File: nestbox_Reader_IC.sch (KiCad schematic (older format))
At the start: 45 parts, among them U2 ST95HF, Y2 ABM11-142-27.120MHz

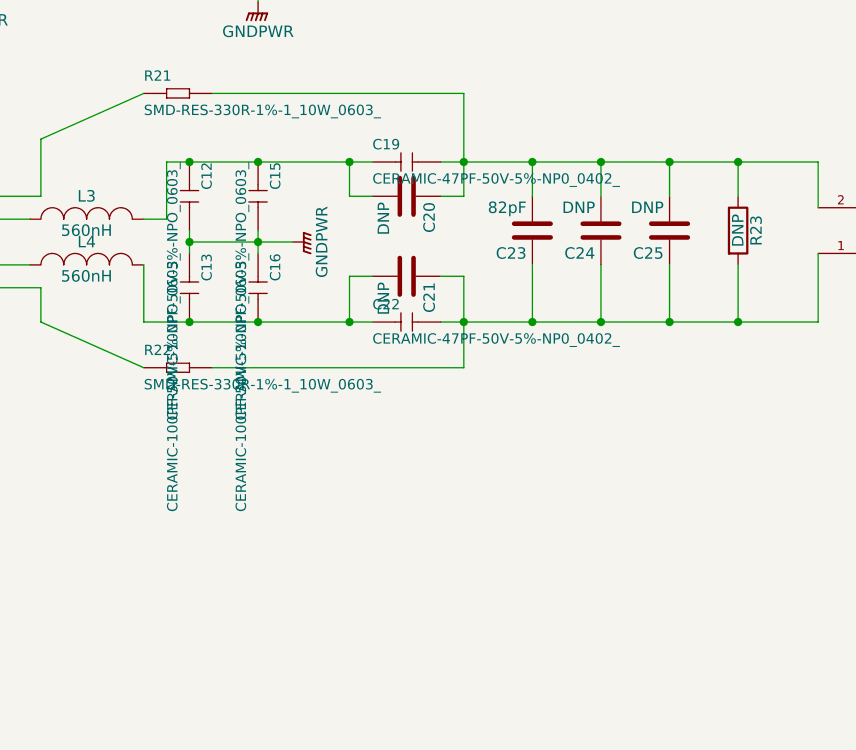
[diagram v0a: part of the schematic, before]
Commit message: Updated BOM with one version of the antenna matching network components
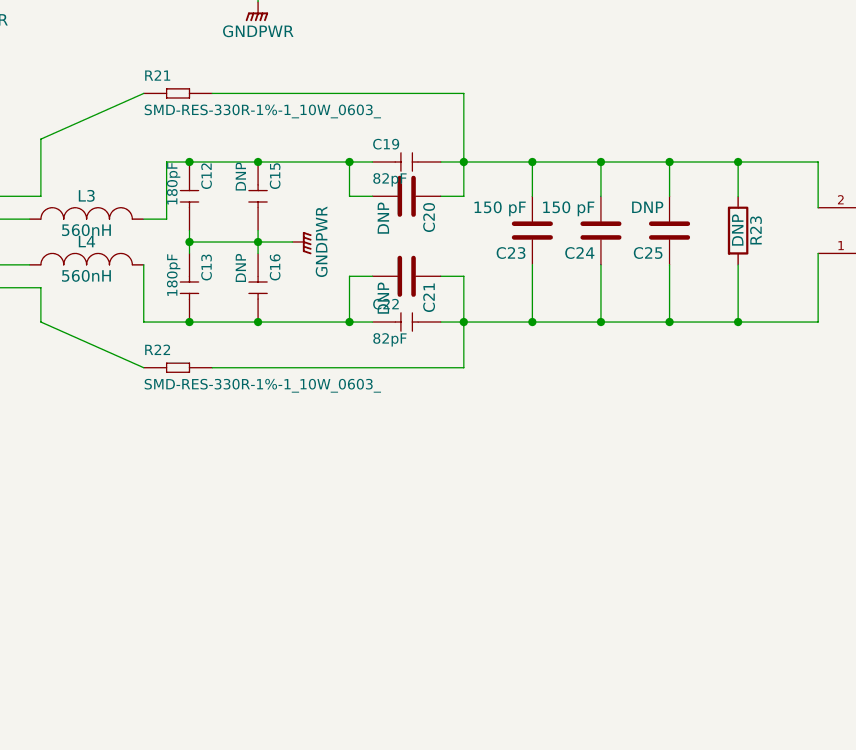
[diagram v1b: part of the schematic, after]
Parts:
- C12, C13: value CERAMIC-100PF-50V-5%-NPO_0603_ -> 180pF
- C15, C16: value CERAMIC-100PF-50V-5%-NPO_0603_ -> DNP
- C19, C22: value CERAMIC-47PF-50V-5%-NP0_0402_ -> 82pF
- C23: value 82pF -> 150 pF
- C24: value DNP -> 150 pF
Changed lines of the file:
@@
 $EndComp
 $Comp
-L GND #PWR44
+L GND #PWR035
 U 1 1 58749360
 P 5300 5750
-F 0 "#PWR44" H 5300 5500 50  0001 C CNN
+F 0 "#PWR035" H 5300 5500 50  0001 C CNN
 F 1 "GND" H 5300 5600 50  0000 C CNN
 F 2 "" H 5300 5750 50  0000 C CNN
@@
 $EndComp
 $Comp
-L GND #PWR43
+L GND #PWR036
 U 1 1 58749377
 P 5200 5750
-F 0 "#PWR43" H 5200 5500 50  0001 C CNN
+F 0 "#PWR036" H 5200 5500 50  0001 C CNN
 F 1 "GND" H 5200 5600 50  0000 C CNN
 F 2 "" H 5200 5750 50  0000 C CNN
@@
 $EndComp
 $Comp
-L GND #PWR47
+L GND #PWR037
 U 1 1 5874938E
 P 5900 5550
-F 0 "#PWR47" H 5900 5300 50  0001 C CNN
+F 0 "#PWR037" H 5900 5300 50  0001 C CNN
 F 1 "GND" H 5900 5400 50  0000 C CNN
 F 2 "" H 5900 5550 50  0000 C CNN
@@
 $EndComp
 $Comp
-L GND #PWR39
+L GND #PWR038
 U 1 1 58749539
 P 4550 6600
-F 0 "#PWR39" H 4550 6350 50  0001 C CNN
+F 0 "#PWR038" H 4550 6350 50  0001 C CNN
 F 1 "GND" H 4550 6450 50  0000 C CNN
 F 2 "" H 4550 6600 50  0000 C CNN
@@
 $EndComp
 $Comp
-L GND #PWR41
+L GND #PWR039
 U 1 1 58749556
 P 4950 5750
-F 0 "#PWR41" H 4950 5500 50  0001 C CNN
+F 0 "#PWR039" H 4950 5500 50  0001 C CNN
 F 1 "GND" H 4950 5600 50  0000 C CNN
 F 2 "" H 4950 5750 50  0000 C CNN
@@
 $EndComp
 $Comp
-L GND #PWR33
+L GND #PWR040
 U 1 1 5874A151
 P 2950 3650
-F 0 "#PWR33" H 2950 3400 50  0001 C CNN
+F 0 "#PWR040" H 2950 3400 50  0001 C CNN
 F 1 "GND" H 2950 3500 50  0000 C CNN
 F 2 "" H 2950 3650 50  0000 C CNN
@@
 $EndComp
 $Comp
-L GND #PWR35
+L GND #PWR041
 U 1 1 5874A18F
 P 3200 3650
-F 0 "#PWR35" H 3200 3400 50  0001 C CNN
+F 0 "#PWR041" H 3200 3400 50  0001 C CNN
 F 1 "GND" H 3200 3500 50  0000 C CNN
 F 2 "" H 3200 3650 50  0000 C CNN
@@
 $EndComp
 $Comp
-L GND #PWR34
+L GND #PWR042
 U 1 1 5874A795
 P 3150 5350
-F 0 "#PWR34" H 3150 5100 50  0001 C CNN
+F 0 "#PWR042" H 3150 5100 50  0001 C CNN
 F 1 "GND" H 3150 5200 50  0000 C CNN
 F 2 "" H 3150 5350 50  0000 C CNN
@@
 $EndComp
 $Comp
-L GND #PWR36
+L GND #PWR043
 U 1 1 5874A7CA
 P 3350 5350
-F 0 "#PWR36" H 3350 5100 50  0001 C CNN
+F 0 "#PWR043" H 3350 5100 50  0001 C CNN
 F 1 "GND" H 3350 5200 50  0000 C CNN
 F 2 "" H 3350 5350 50  0000 C CNN
@@
 $EndComp
 $Comp
-L GND #PWR40
+L GND #PWR044
 U 1 1 5874B119
 P 4600 2950
-F 0 "#PWR40" H 4600 2700 50  0001 C CNN
+F 0 "#PWR044" H 4600 2700 50  0001 C CNN
 F 1 "GND" H 4600 2800 50  0000 C CNN
 F 2 "" H 4600 2950 50  0000 C CNN
@@
 $EndComp
 $Comp
-L GND #PWR38
+L GND #PWR045
 U 1 1 5874B903
 P 4550 5850
-F 0 "#PWR38" H 4550 5600 50  0001 C CNN
+F 0 "#PWR045" H 4550 5600 50  0001 C CNN
 F 1 "GND" H 4550 5700 50  0000 C CNN
 F 2 "" H 4550 5850 50  0000 C CNN
@@
 P 7050 3850
 F 0 "C12" H 6900 3900 45  0000 L BNN
-F 1 "CERAMIC-100PF-50V-5%-NPO_0603_" H 6900 3750 45  0000 L BNN
+F 1 "180pF" H 6900 3750 45  0000 L BNN
 F 2 "SeeedOPL-Capacitor-2016:C0603" H 7050 3850 60  0001 C CNN
 F 3 "" H 7050 3850 60  0001 C CNN
@@
 P 7050 4250
 F 0 "C13" H 6900 4300 45  0000 L BNN
-F 1 "CERAMIC-100PF-50V-5%-NPO_0603_" H 6900 4150 45  0000 L BNN
+F 1 "180pF" H 6900 4150 45  0000 L BNN
 F 2 "SeeedOPL-Capacitor-2016:C0603" H 7050 4250 60  0001 C CNN
 F 3 "" H 7050 4250 60  0001 C CNN
@@
 $EndComp
 $Comp
-L CERAMIC-100PF-50V-5%-NPO_0603_ C15
-U 1 1 5874CA5E
-P 7350 3850
-F 0 "C15" H 7200 3900 45  0000 L BNN
-F 1 "CERAMIC-100PF-50V-5%-NPO_0603_" H 7200 3750 45  0000 L BNN
-F 2 "SeeedOPL-Capacitor-2016:C0603" H 7350 3850 60  0001 C CNN
-F 3 "" H 7350 3850 60  0001 C CNN
-F 4 "CC0603JRNPO9BN101" H 7380 4000 20  0001 C CNN "MPN"
-F 5 "302010076" H 7380 4000 20  0001 C CNN "SKU"
-F 6 "" H 7380 4000 20  0001 C CNN "Field6"
-	1    7350 3850
-	0    1    1    0
-$EndComp
-$Comp
 L CERAMIC-100PF-50V-5%-NPO_0603_ C16
 U 1 1 5874CAD9
 P 7350 4250
 F 0 "C16" H 7200 4300 45  0000 L BNN
-F 1 "CERAMIC-100PF-50V-5%-NPO_0603_" H 7200 4150 45  0000 L BNN
+F 1 "DNP" H 7200 4150 45  0000 L BNN
 F 2 "SeeedOPL-Capacitor-2016:C0603" H 7350 4250 60  0001 C CNN
 F 3 "" H 7350 4250 60  0001 C CNN
@@
 P 8000 3700
 F 0 "C19" H 7850 3750 45  0000 L BNN
-F 1 "CERAMIC-47PF-50V-5%-NP0_0402_" H 7850 3600 45  0000 L BNN
+F 1 "82pF" H 7850 3600 45  0000 L BNN
 F 2 "SeeedOPL-Capacitor-2016:C0402" H 8000 3700 60  0001 C CNN
 F 3 "" H 8000 3700 60  0001 C CNN
@@
 P 8000 4400
 F 0 "C22" H 7850 4450 45  0000 L BNN
-F 1 "CERAMIC-47PF-50V-5%-NP0_0402_" H 7850 4300 45  0000 L BNN
+F 1 "82pF" H 7850 4300 45  0000 L BNN
 F 2 "SeeedOPL-Capacitor-2016:C0402" H 8000 4400 60  0001 C CNN
 F 3 "" H 8000 4400 60  0001 C CNN
@@
 P 8850 4000
 F 0 "C24" H 8875 4100 50  0000 L CNN
-F 1 "DNP" H 8875 3900 50  0000 L CNN
+F 1 "150 pF" H 8875 3900 50  0000 L CNN
 F 2 "Capacitors_SMD:C_0603" H 8888 3850 50  0001 C CNN
 F 3 "" H 8850 4000 50  0000 C CNN
@@
 P 8550 4000
 F 0 "C23" H 8575 4100 50  0000 L CNN
-F 1 "82pF" H 8575 3900 50  0000 L CNN
+F 1 "150 pF" H 8575 3900 50  0000 L CNN
 F 2 "Capacitors_SMD:C_0603" H 8588 3850 50  0001 C CNN
 F 3 "" H 8550 4000 50  0000 C CNN
@@
 Connection ~ 5450 1950
 $Comp
-L GND #PWR46
+L GND #PWR046
 U 1 1 58757B97
 P 5550 1950
-F 0 "#PWR46" H 5550 1700 50  0001 C CNN
+F 0 "#PWR046" H 5550 1700 50  0001 C CNN
 F 1 "GND" H 5550 1800 50  0000 C CNN
 F 2 "" H 5550 1950 50  0000 C CNN
@@
 needed to wakeup from \nhybernate state
 $Comp
-L GNDPWR #PWR45
+L GNDPWR #PWR047
 U 1 1 5877A1C6
 P 5350 3550
-F 0 "#PWR45" H 5350 3350 50  0001 C CNN
+F 0 "#PWR047" H 5350 3350 50  0001 C CNN
 F 1 "GNDPWR" H 5350 3420 50  0000 C CNN
 F 2 "" H 5350 3500 50  0000 C CNN
@@
 $EndComp
 $Comp
-L GNDPWR #PWR48
+L GNDPWR #PWR048
 U 1 1 5877A6A8
 P 6100 2950
-F 0 "#PWR48" H 6100 2750 50  0001 C CNN
+F 0 "#PWR048" H 6100 2750 50  0001 C CNN
 F 1 "GNDPWR" H 6100 2820 50  0000 C CNN
 F 2 "" H 6100 2900 50  0000 C CNN
@@
 $EndComp
 $Comp
-L GNDPWR #PWR50
+L GNDPWR #PWR049
 U 1 1 5877A73A
 P 7350 3000
-F 0 "#PWR50" H 7350 2800 50  0001 C CNN
+F 0 "#PWR049" H 7350 2800 50  0001 C CNN
 F 1 "GNDPWR" H 7350 2870 50  0000 C CNN
 F 2 "" H 7350 2950 50  0000 C CNN
@@
 $EndComp
 $Comp
-L GNDPWR #PWR51
+L GNDPWR #PWR050
 U 1 1 5877A7CC
 P 7500 4050
-F 0 "#PWR51" H 7500 3850 50  0001 C CNN
+F 0 "#PWR050" H 7500 3850 50  0001 C CNN
 F 1 "GNDPWR" H 7500 3920 50  0000 C CNN
 F 2 "" H 7500 4000 50  0000 C CNN
@@
 	6100 2950 6100 2900
 $Comp
-L +3.3V #PWR42
+L +3.3V #PWR051
 U 1 1 587A13E4
 P 5150 1000
-F 0 "#PWR42" H 5150 850 50  0001 C CNN
+F 0 "#PWR051" H 5150 850 50  0001 C CNN
 F 1 "+3.3V" H 5150 1140 50  0000 C CNN
 F 2 "" H 5150 1000 50  0000 C CNN
@@
 	5150 1000 5150 1150
 $Comp
-L VDDA #PWR49
+L VDDA #PWR052
 U 1 1 587A16E6
 P 7200 1000
-F 0 "#PWR49" H 7200 850 50  0001 C CNN
+F 0 "#PWR052" H 7200 850 50  0001 C CNN
 F 1 "VDDA" H 7200 1150 50  0000 C CNN
 F 2 "" H 7200 1000 50  0000 C CNN
@@
 $EndComp
 $Comp
-L +3.3V #PWR37
+L +3.3V #PWR053
 U 1 1 587A19B2
 P 3800 3400
-F 0 "#PWR37" H 3800 3250 50  0001 C CNN
+F 0 "#PWR053" H 3800 3250 50  0001 C CNN
 F 1 "+3.3V" H 3800 3540 50  0000 C CNN
 F 2 "" H 3800 3400 50  0000 C CNN
@@
 $EndComp
 $Comp
-L +3.3V #PWR32
+L +3.3V #PWR054
 U 1 1 587A1A44
 P 2950 2400
-F 0 "#PWR32" H 2950 2250 50  0001 C CNN
+F 0 "#PWR054" H 2950 2250 50  0001 C CNN
 F 1 "+3.3V" H 2950 2540 50  0000 C CNN
 F 2 "" H 2950 2400 50  0000 C CNN
@@
 $EndComp
 $Comp
-L +3.3V #PWR31
+L +3.3V #PWR055
 U 1 1 587A1D85
 P 2700 6300
-F 0 "#PWR31" H 2700 6150 50  0001 C CNN
+F 0 "#PWR055" H 2700 6150 50  0001 C CNN
 F 1 "+3.3V" H 2700 6440 50  0000 C CNN
 F 2 "" H 2700 6300 50  0000 C CNN
@@
 Wire Wire Line
 	7200 1650 7200 1800
+$Comp
+L CERAMIC-100PF-50V-5%-NPO_0603_ C15
+U 1 1 5874CA5E
+P 7350 3850
+F 0 "C15" H 7200 3900 45  0000 L BNN
+F 1 "DNP" H 7200 3750 45  0000 L BNN
+F 2 "SeeedOPL-Capacitor-2016:C0603" H 7350 3850 60  0001 C CNN
+F 3 "" H 7350 3850 60  0001 C CNN
+F 4 "CC0603JRNPO9BN101" H 7380 4000 20  0001 C CNN "MPN"
+F 5 "302010076" H 7380 4000 20  0001 C CNN "SKU"
+F 6 "" H 7380 4000 20  0001 C CNN "Field6"
+	1    7350 3850
+	0    1    1    0
+$EndComp
 $EndSCHEMATC
